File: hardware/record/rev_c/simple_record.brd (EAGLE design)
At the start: 34.9 x 30 mm, 25 parts, among them J1 PJ-035C, J2 SCREW-TERMINAL_2_0.100, J3 SCREW-TERMINAL_2_0.100, J4 SQUALL_HEADER, J5 PJ-102AH, Q1 MOSFET-NCHANNELSMD, U1 MAX44284

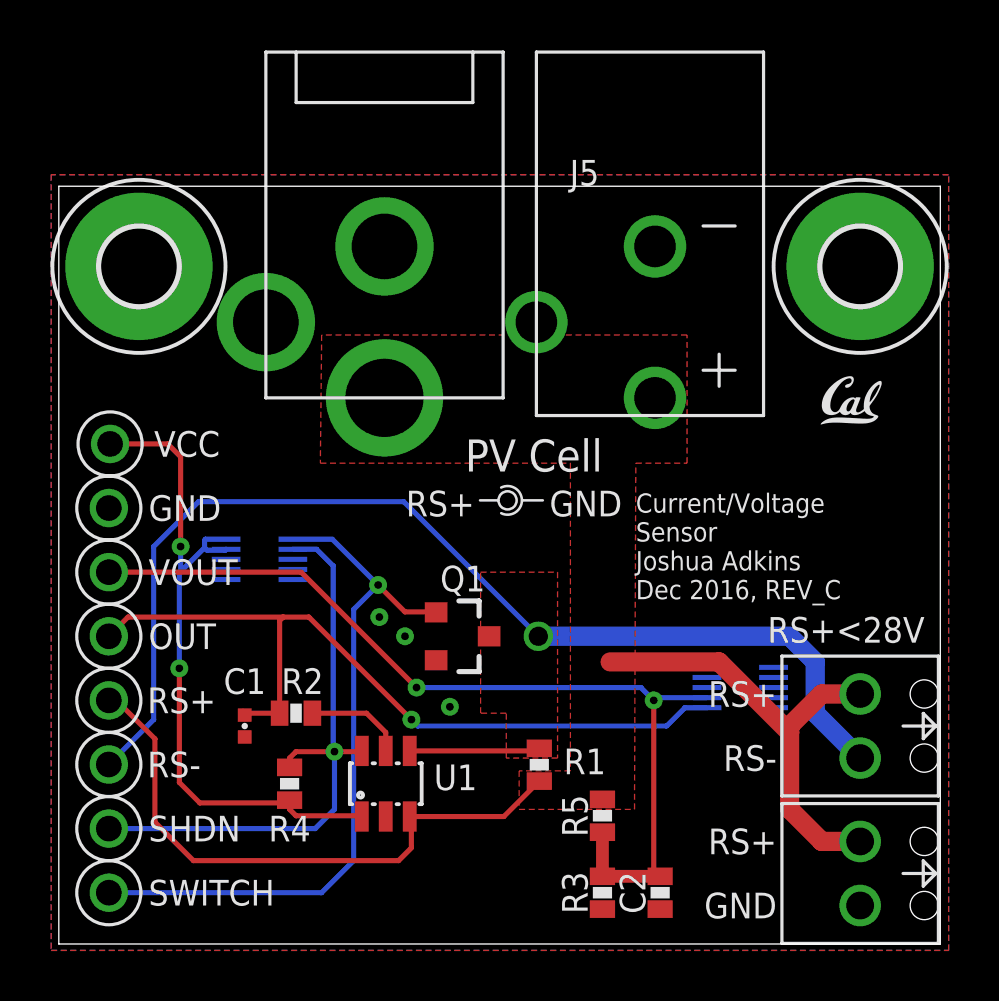
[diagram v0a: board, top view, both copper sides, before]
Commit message: Cleaned up some silkscreen, lined up VCC TP
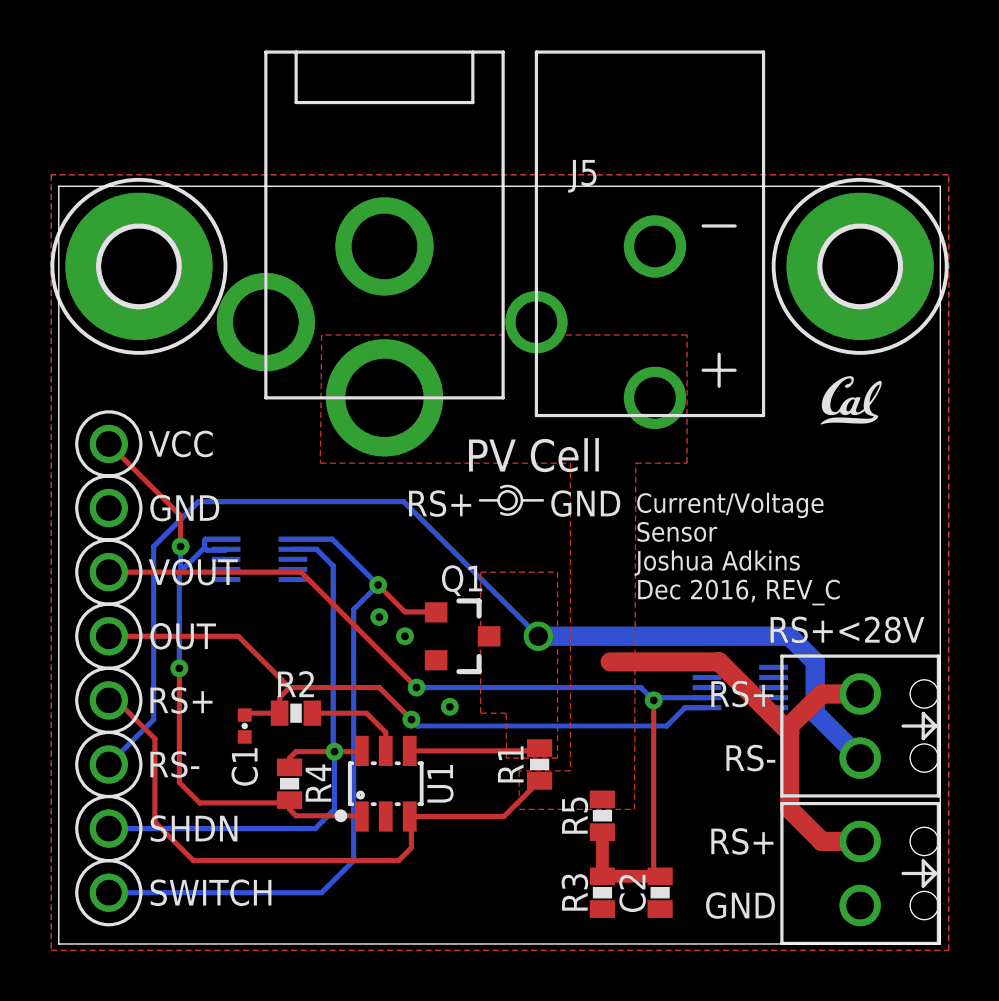
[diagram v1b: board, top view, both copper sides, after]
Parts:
- moved TP8 0.05 mm to (1.98, 19.8)
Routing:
- net OUT: track 31.6 -> 28.3 mm
- net VCC: track 27.5 -> 26.1 mm
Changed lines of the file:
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@@
 <setting verticaltext="up"/>
 </settings>
-<grid distance="0.1" unitdist="inch" unit="inch" style="lines" multiple="1" display="yes" altdistance="0.01" altunitdist="inch" altunit="inch"/>
+<grid distance="10" unitdist="mil" unit="mil" style="lines" multiple="1" display="yes" altdistance="0.01" altunitdist="inch" altunit="inch"/>
 <layers>
 <layer number="1" name="Top" color="4" fill="1" visible="yes" active="yes"/>
@@
 <text x="3.556" y="2.032" size="1.016" layer="25" font="vector" ratio="12" align="center-left">SWITCH</text>
 <text x="31.1912" y="11.938" size="1.016" layer="25" font="vector" ratio="12" align="bottom-center">RS+&lt;28V</text>
-<text x="5.08" y="19.304" size="1.016" layer="21" font="vector" ratio="12" align="bottom-center">VCC</text>
+<text x="3.556" y="19.812" size="1.016" layer="21" font="vector" ratio="12" align="center-left">VCC</text>
+<circle x="11.176" y="5.08" radius="0.254" width="0" layer="21"/>
 </plain>
 <attributes>
@@
 <attribute name="NAME" x="23.241" y="2.032" size="1.016" layer="25" font="vector" ratio="12" rot="R90" align="bottom-center"/>
 </element>
-<element name="R1" library="passives" package="0603-RES" value="0.06" x="19.0372" y="7.104" smashed="yes" rot="R270">
-<attribute name="NAME" x="20.8392" y="6.726" size="1.016" layer="25" font="vector" ratio="12" align="bottom-center"/>
+<element name="R1" library="passives" package="0603-RES" value="0.06" x="19.05" y="7.112" smashed="yes" rot="R270">
+<attribute name="NAME" x="18.415" y="7.112" size="1.016" layer="25" font="vector" ratio="12" rot="R270" align="top-center"/>
 </element>
 <element name="J4" library="squall" package="SQUALL_HEADER" value="SQUALL_HEADER" x="17.4752" y="12.7" smashed="yes">
@@
 <element name="U1" library="chips" package="SOT-23-6" value="MAX44284" x="12.954" y="6.35" smashed="yes">
 <attribute name="DIGIKEY" value="MAX44284FAUT+TCT-ND" x="12.954" y="6.35" size="1.778" layer="27" font="vector" ratio="12" display="off"/>
-<attribute name="NAME" x="14.859" y="6.096" size="1.016" layer="25" font="vector" ratio="12"/>
+<attribute name="NAME" x="14.605" y="6.35" size="1.016" layer="25" font="vector" ratio="12" rot="R90" align="top-center"/>
 <attribute name="VALUE" x="11.049" y="2.54" size="1.27" layer="27" font="vector"/>
 </element>
 <element name="C1" library="passives" package="0402_CAP" value="2.2nF" x="7.366" y="8.636" smashed="yes" rot="R270">
-<attribute name="NAME" x="7.366" y="9.906" size="1.016" layer="25" font="vector" ratio="12" align="bottom-center"/>
+<attribute name="NAME" x="7.366" y="7.874" size="1.016" layer="25" font="vector" ratio="12" rot="R90" align="center-right"/>
 <attribute name="VALUE" x="5.969" y="8.636" size="1.016" layer="27" font="vector" ratio="12" rot="R270" align="bottom-center"/>
 </element>
 <element name="R2" library="passives" package="0603-RES" value="1.8k" x="9.398" y="9.144" smashed="yes">
-<attribute name="NAME" x="9.652" y="9.906" size="1.016" layer="25" font="vector" ratio="12" align="bottom-center"/>
+<attribute name="NAME" x="9.398" y="9.779" size="1.016" layer="25" font="vector" ratio="12" align="bottom-center"/>
 </element>
 <element name="R4" library="passives" package="0603-RES" value="100k" x="9.144" y="6.35" smashed="yes" rot="R270">
-<attribute name="NAME" x="9.144" y="4.064" size="1.016" layer="25" font="vector" ratio="12" align="bottom-center"/>
-</element>
-<element name="TP8" library="headers" package="TESTPOINT_0.040IN" value="TEST_POINT_0.040IN" x="2.032" y="19.812" smashed="yes">
-<attribute name="DIGIKEY" value="5001K-ND" x="2.032" y="19.812" size="1.778" layer="27" font="vector" ratio="12" display="off"/>
-<attribute name="VALUE" x="2.032" y="17.272" size="1.016" layer="27" font="vector" ratio="12" align="bottom-center"/>
+<attribute name="NAME" x="9.779" y="6.35" size="1.016" layer="25" font="vector" ratio="12" rot="R90" align="top-center"/>
+</element>
+<element name="TP8" library="headers" package="TESTPOINT_0.040IN" value="TEST_POINT_0.040IN" x="1.9812" y="19.812" smashed="yes">
+<attribute name="DIGIKEY" value="5001K-ND" x="1.9812" y="19.812" size="1.778" layer="27" font="vector" ratio="12" display="off"/>
+<attribute name="VALUE" x="1.9812" y="17.272" size="1.016" layer="27" font="vector" ratio="12" align="bottom-center"/>
 </element>
 </elements>
@@
 <contactref element="U1" pad="3"/>
 <wire x1="13.904" y1="5.05" x2="17.6332" y2="5.05" width="0.2032" layer="1"/>
-<wire x1="17.6332" y1="5.05" x2="19.0372" y2="6.454" width="0.2032" layer="1"/>
+<wire x1="17.6332" y1="5.05" x2="19.05" y2="6.462" width="0.2032" layer="1"/>
 <wire x1="1.9812" y1="9.652" x2="2.286" y2="9.652" width="0.2032" layer="1"/>
 <wire x1="2.286" y1="9.652" x2="3.81" y2="8.128" width="0.2032" layer="1"/>
@@
 <via x="4.7752" y="10.922" extent="1-16" drill="0.3048"/>
 <wire x1="4.7752" y1="10.922" x2="4.7752" y2="14.7" width="0.2032" layer="16"/>
-<wire x1="4.7752" y1="14.7" x2="4.8166" y2="14.7414" width="0.2032" layer="16"/>
+<wire x1="4.7752" y1="14.7" x2="4.826" y2="14.7508" width="0.2032" layer="16"/>
 <contactref element="U1" pad="1"/>
 <contactref element="R4" pad="2"/>
@@
 <wire x1="9.032" y1="5.588" x2="9.144" y2="5.7" width="0.2032" layer="1"/>
 <contactref element="TP8" pad="TESTPOINT"/>
-<wire x1="2.032" y1="19.812" x2="4.318" y2="19.812" width="0.2032" layer="1"/>
-<wire x1="4.318" y1="19.812" x2="4.826" y2="19.304" width="0.2032" layer="1"/>
-<wire x1="4.826" y1="19.304" x2="4.826" y2="15.748" width="0.2032" layer="1"/>
 <via x="4.826" y="15.748" extent="1-16" drill="0.3048"/>
 <wire x1="4.826" y1="15.748" x2="4.826" y2="14.7508" width="0.2032" layer="16"/>
-<wire x1="4.826" y1="14.7508" x2="4.8166" y2="14.7414" width="0.2032" layer="16"/>
+<wire x1="4.826" y1="15.748" x2="4.826" y2="16.9672" width="0.2032" layer="1"/>
+<wire x1="4.826" y1="16.9672" x2="1.9812" y2="19.812" width="0.2032" layer="1"/>
 </signal>
 <signal name="VOUT">
@@
 <wire x1="25.6802" y1="9.36" x2="24.8032" y2="9.36" width="0.2032" layer="16"/>
 <wire x1="24.8032" y1="9.36" x2="24.0792" y2="8.636" width="0.2032" layer="16"/>
-<wire x1="9.906" y1="12.954" x2="8.89" y2="12.954" width="0.2032" layer="1"/>
 <contactref element="R2" pad="1"/>
 <contactref element="C1" pad="1"/>
 <contactref element="TP7" pad="TESTPOINT"/>
-<wire x1="8.89" y1="12.954" x2="2.7432" y2="12.954" width="0.2032" layer="1"/>
-<wire x1="2.7432" y1="12.954" x2="1.9812" y2="12.192" width="0.2032" layer="1"/>
 <wire x1="7.366" y1="9.06906875" x2="7.29106875" y2="9.21893125" width="0.2032" layer="1"/>
 <wire x1="7.29106875" y1="9.21893125" x2="7.366" y2="9.144" width="0.2032" layer="1"/>
 <wire x1="7.366" y1="9.144" x2="8.748" y2="9.144" width="0.2032" layer="1"/>
-<wire x1="9.906" y1="12.954" x2="13.97" y2="8.89" width="0.2032" layer="1"/>
 <via x="13.97" y="8.89" extent="1-16" drill="0.3048"/>
 <wire x1="13.97" y1="8.89" x2="14.224" y2="8.636" width="0.2032" layer="16"/>
 <wire x1="14.224" y1="8.636" x2="24.0792" y2="8.636" width="0.2032" layer="16"/>
-<wire x1="8.748" y1="9.144" x2="8.748" y2="12.812" width="0.2032" layer="1"/>
-<wire x1="8.748" y1="12.812" x2="8.89" y2="12.954" width="0.2032" layer="1"/>
+<wire x1="13.97" y1="8.89" x2="12.7" y2="10.16" width="0.2032" layer="1"/>
+<wire x1="12.7" y1="10.16" x2="9.144" y2="10.16" width="0.2032" layer="1"/>
+<wire x1="9.144" y1="10.16" x2="8.748" y2="9.764" width="0.2032" layer="1"/>
+<wire x1="8.748" y1="9.764" x2="8.748" y2="9.144" width="0.2032" layer="1"/>
+<wire x1="1.9812" y1="12.192" x2="7.112" y2="12.192" width="0.2032" layer="1"/>
+<wire x1="7.112" y1="12.192" x2="9.144" y2="10.16" width="0.2032" layer="1"/>
 </signal>
 <signal name="SHDN">
@@
 <contactref element="TP6" pad="TESTPOINT"/>
 <contactref element="J3" pad="1"/>
-<wire x1="18.9172" y1="7.874" x2="19.0372" y2="7.754" width="0.254" layer="1"/>
-<wire x1="18.9992" y1="7.792" x2="19.0372" y2="7.754" width="0.254" layer="1"/>
+<wire x1="18.9172" y1="7.874" x2="19.05" y2="7.762" width="0.254" layer="1"/>
+<wire x1="18.9992" y1="7.792" x2="19.05" y2="7.762" width="0.254" layer="1"/>
 <polygon width="0.2032" layer="1" isolate="0.3048" thermals="no">
 <vertex x="19.7612" y="7.366"/>
@@
 <contactref element="U1" pad="4"/>
 <wire x1="13.904" y1="7.65" x2="18.8872" y2="7.65" width="0.2032" layer="1"/>
-<wire x1="18.8872" y1="7.65" x2="19.0372" y2="7.754" width="0.2032" layer="1"/>
+<wire x1="18.8872" y1="7.65" x2="19.05" y2="7.762" width="0.2032" layer="1"/>
 </signal>
 <signal name="N$1">
